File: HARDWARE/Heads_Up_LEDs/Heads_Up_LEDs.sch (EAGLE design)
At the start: 10 parts, among them J1 TRRS

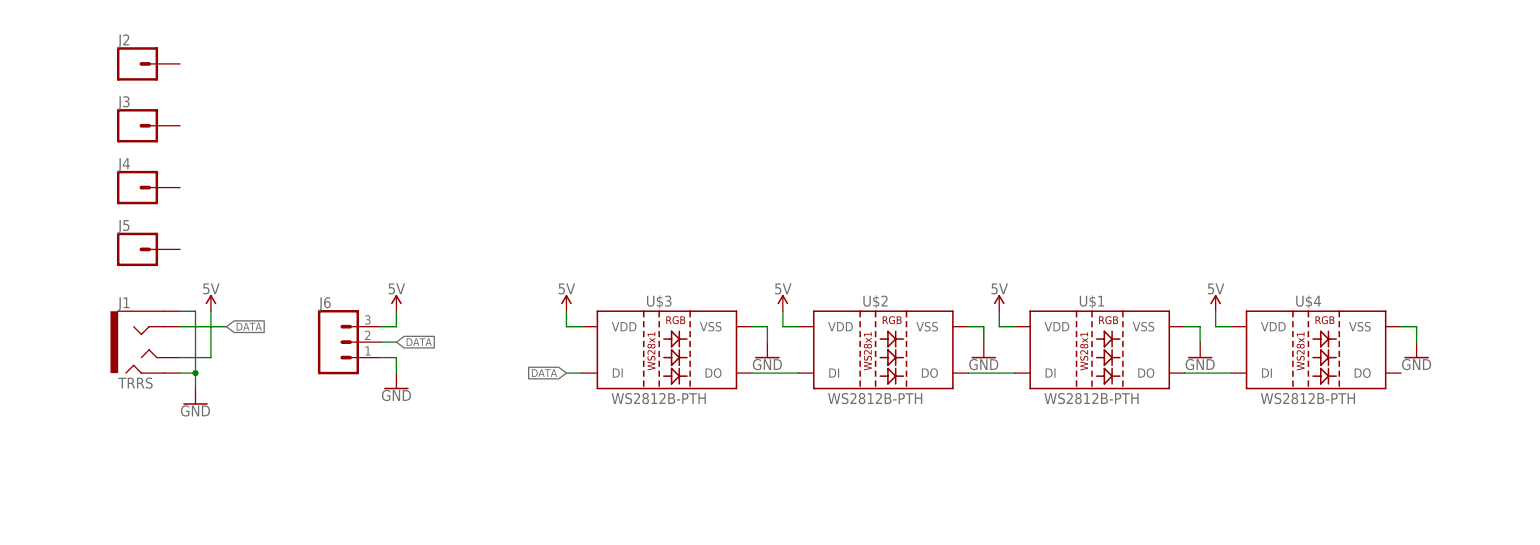
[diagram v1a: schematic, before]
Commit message: fixed ws2812 pinouts - added res and cap
library for ws2812 pth pinout was incorrect. I also added in a cap and resistor like the hookup guide suggests. Not sure if necessary, cuz the protos of v01 are working without (although I had to rotate the LEDs 180 degrees.
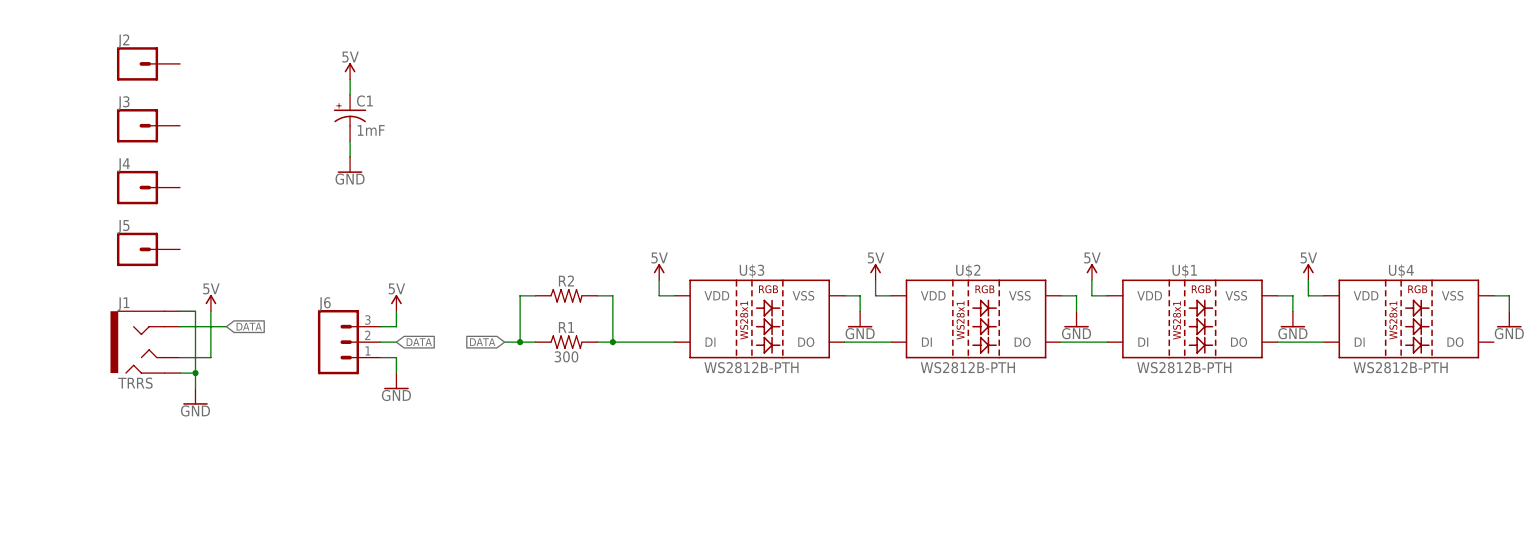
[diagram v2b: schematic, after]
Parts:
- added C1: 1mF, SparkFun-Capacitors:1000UF-RADIAL-5MM-25V-20%
- added R1: 300, SparkFun-Resistors:300OHM-0603-1/10W-1%
- added R2: (no value), SparkFun-Resistors:RESISTORAXIAL-0.3
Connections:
- new net N$2: R1.2, R2.2, U$3.DI
- net 5V: now also C1.+
- net DATA: now also R1.1, R2.1; no longer U$3.DI
- net GND: now also C1.-
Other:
- moved on the sheet: U$1, U$2, U$3, U$4
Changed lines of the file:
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@@
 <part name="SUPPLY6" library="SparkFun-PowerSymbols" deviceset="5V" device=""/>
 <part name="GND6" library="SparkFun-PowerSymbols" deviceset="GND" device=""/>
+<part name="R1" library="SparkFun-Resistors" deviceset="300OHM" device="-0603-1/10W-1%" value="300"/>
+<part name="R2" library="SparkFun-Resistors" deviceset="RESISTOR" device="AXIAL-0.3" value=" "/>
+<part name="C1" library="SparkFun-Capacitors" deviceset="1000UF" device="-RADIAL-5MM-25V-20%" value="1mF"/>
+<part name="GND7" library="SparkFun-PowerSymbols" deviceset="GND" device=""/>
+<part name="SUPPLY7" library="SparkFun-PowerSymbols" deviceset="5V" device=""/>
 </parts>
 <sheets>
@@
 <instances>
 <instance part="J1" gate="G$1" x="40.64" y="55.88"/>
-<instance part="U$1" gate="G$1" x="198.12" y="53.34"/>
-<instance part="U$2" gate="G$1" x="162.56" y="53.34"/>
-<instance part="U$3" gate="G$1" x="127" y="53.34"/>
+<instance part="U$1" gate="G$1" x="213.36" y="58.42"/>
+<instance part="U$2" gate="G$1" x="177.8" y="58.42"/>
+<instance part="U$3" gate="G$1" x="142.24" y="58.42"/>
 <instance part="J2" gate="G$1" x="38.1" y="101.6"/>
 <instance part="J3" gate="G$1" x="38.1" y="91.44"/>
@@
 <instance part="J5" gate="G$1" x="38.1" y="71.12"/>
 <instance part="J6" gate="J$1" x="71.12" y="55.88"/>
-<instance part="SUPPLY1" gate="G$1" x="109.22" y="60.96"/>
-<instance part="SUPPLY2" gate="G$1" x="144.78" y="60.96"/>
-<instance part="SUPPLY3" gate="G$1" x="180.34" y="60.96"/>
+<instance part="SUPPLY1" gate="G$1" x="124.46" y="66.04"/>
+<instance part="SUPPLY2" gate="G$1" x="160.02" y="66.04"/>
+<instance part="SUPPLY3" gate="G$1" x="195.58" y="66.04"/>
 <instance part="SUPPLY4" gate="G$1" x="50.8" y="60.96"/>
 <instance part="GND1" gate="1" x="48.26" y="45.72"/>
-<instance part="GND2" gate="1" x="142.24" y="53.34"/>
-<instance part="GND3" gate="1" x="177.8" y="53.34"/>
-<instance part="GND4" gate="1" x="213.36" y="53.34"/>
+<instance part="GND2" gate="1" x="157.48" y="58.42"/>
+<instance part="GND3" gate="1" x="193.04" y="58.42"/>
+<instance part="GND4" gate="1" x="228.6" y="58.42"/>
 <instance part="GND5" gate="1" x="81.28" y="48.26"/>
 <instance part="SUPPLY5" gate="G$1" x="81.28" y="60.96"/>
-<instance part="U$4" gate="G$1" x="233.68" y="53.34"/>
-<instance part="SUPPLY6" gate="G$1" x="215.9" y="60.96"/>
-<instance part="GND6" gate="1" x="248.92" y="53.34"/>
+<instance part="U$4" gate="G$1" x="248.92" y="58.42"/>
+<instance part="SUPPLY6" gate="G$1" x="231.14" y="66.04"/>
+<instance part="GND6" gate="1" x="264.16" y="58.42"/>
+<instance part="R1" gate="G$1" x="109.22" y="55.88"/>
+<instance part="R2" gate="G$1" x="109.22" y="63.5"/>
+<instance part="C1" gate="G$1" x="73.66" y="93.98"/>
+<instance part="GND7" gate="1" x="73.66" y="83.82"/>
+<instance part="SUPPLY7" gate="G$1" x="73.66" y="99.06"/>
 </instances>
 <busses>
@@
 <pinref part="U$3" gate="G$1" pin="DO"/>
 <pinref part="U$2" gate="G$1" pin="DI"/>
-<wire x1="139.7" y1="50.8" x2="147.32" y2="50.8" width="0.1524" layer="91"/>
+<wire x1="154.94" y1="55.88" x2="162.56" y2="55.88" width="0.1524" layer="91"/>
 </segment>
 </net>
@@
 <pinref part="U$2" gate="G$1" pin="DO"/>
 <pinref part="U$1" gate="G$1" pin="DI"/>
-<wire x1="175.26" y1="50.8" x2="182.88" y2="50.8" width="0.1524" layer="91"/>
+<wire x1="190.5" y1="55.88" x2="198.12" y2="55.88" width="0.1524" layer="91"/>
 </segment>
 </net>
@@
 <segment>
 <pinref part="U$3" gate="G$1" pin="VDD"/>
-<wire x1="111.76" y1="58.42" x2="109.22" y2="58.42" width="0.1524" layer="91"/>
-<wire x1="109.22" y1="58.42" x2="109.22" y2="60.96" width="0.1524" layer="91"/>
+<wire x1="127" y1="63.5" x2="124.46" y2="63.5" width="0.1524" layer="91"/>
+<wire x1="124.46" y1="63.5" x2="124.46" y2="66.04" width="0.1524" layer="91"/>
 <pinref part="SUPPLY1" gate="G$1" pin="5V"/>
 </segment>
 <segment>
 <pinref part="U$2" gate="G$1" pin="VDD"/>
-<wire x1="147.32" y1="58.42" x2="144.78" y2="58.42" width="0.1524" layer="91"/>
-<wire x1="144.78" y1="58.42" x2="144.78" y2="60.96" width="0.1524" layer="91"/>
+<wire x1="162.56" y1="63.5" x2="160.02" y2="63.5" width="0.1524" layer="91"/>
+<wire x1="160.02" y1="63.5" x2="160.02" y2="66.04" width="0.1524" layer="91"/>
 <pinref part="SUPPLY2" gate="G$1" pin="5V"/>
 </segment>
 <segment>
 <pinref part="U$1" gate="G$1" pin="VDD"/>
-<wire x1="182.88" y1="58.42" x2="180.34" y2="58.42" width="0.1524" layer="91"/>
-<wire x1="180.34" y1="58.42" x2="180.34" y2="60.96" width="0.1524" layer="91"/>
+<wire x1="198.12" y1="63.5" x2="195.58" y2="63.5" width="0.1524" layer="91"/>
+<wire x1="195.58" y1="63.5" x2="195.58" y2="66.04" width="0.1524" layer="91"/>
 <pinref part="SUPPLY3" gate="G$1" pin="5V"/>
 </segment>
@@
 <segment>
 <pinref part="U$4" gate="G$1" pin="VDD"/>
-<wire x1="218.44" y1="58.42" x2="215.9" y2="58.42" width="0.1524" layer="91"/>
-<wire x1="215.9" y1="58.42" x2="215.9" y2="60.96" width="0.1524" layer="91"/>
+<wire x1="233.68" y1="63.5" x2="231.14" y2="63.5" width="0.1524" layer="91"/>
+<wire x1="231.14" y1="63.5" x2="231.14" y2="66.04" width="0.1524" layer="91"/>
 <pinref part="SUPPLY6" gate="G$1" pin="5V"/>
+</segment>
+<segment>
+<pinref part="SUPPLY7" gate="G$1" pin="5V"/>
+<wire x1="73.66" y1="96.52" x2="73.66" y2="99.06" width="0.1524" layer="91"/>
+<pinref part="C1" gate="G$1" pin="+"/>
 </segment>
 </net>
@@
 <segment>
 <pinref part="U$3" gate="G$1" pin="VSS"/>
-<wire x1="139.7" y1="58.42" x2="142.24" y2="58.42" width="0.1524" layer="91"/>
-<wire x1="142.24" y1="58.42" x2="142.24" y2="55.88" width="0.1524" layer="91"/>
+<wire x1="154.94" y1="63.5" x2="157.48" y2="63.5" width="0.1524" layer="91"/>
+<wire x1="157.48" y1="63.5" x2="157.48" y2="60.96" width="0.1524" layer="91"/>
 <pinref part="GND2" gate="1" pin="GND"/>
 </segment>
 <segment>
 <pinref part="U$2" gate="G$1" pin="VSS"/>
-<wire x1="175.26" y1="58.42" x2="177.8" y2="58.42" width="0.1524" layer="91"/>
-<wire x1="177.8" y1="58.42" x2="177.8" y2="55.88" width="0.1524" layer="91"/>
+<wire x1="190.5" y1="63.5" x2="193.04" y2="63.5" width="0.1524" layer="91"/>
+<wire x1="193.04" y1="63.5" x2="193.04" y2="60.96" width="0.1524" layer="91"/>
 <pinref part="GND3" gate="1" pin="GND"/>
 </segment>
 <segment>
 <pinref part="U$1" gate="G$1" pin="VSS"/>
-<wire x1="210.82" y1="58.42" x2="213.36" y2="58.42" width="0.1524" layer="91"/>
-<wire x1="213.36" y1="58.42" x2="213.36" y2="55.88" width="0.1524" layer="91"/>
+<wire x1="226.06" y1="63.5" x2="228.6" y2="63.5" width="0.1524" layer="91"/>
+<wire x1="228.6" y1="63.5" x2="228.6" y2="60.96" width="0.1524" layer="91"/>
 <pinref part="GND4" gate="1" pin="GND"/>
 </segment>
@@
 <segment>
 <pinref part="U$4" gate="G$1" pin="VSS"/>
-<wire x1="246.38" y1="58.42" x2="248.92" y2="58.42" width="0.1524" layer="91"/>
-<wire x1="248.92" y1="58.42" x2="248.92" y2="55.88" width="0.1524" layer="91"/>
+<wire x1="261.62" y1="63.5" x2="264.16" y2="63.5" width="0.1524" layer="91"/>
+<wire x1="264.16" y1="63.5" x2="264.16" y2="60.96" width="0.1524" layer="91"/>
 <pinref part="GND6" gate="1" pin="GND"/>
+</segment>
+<segment>
+<pinref part="C1" gate="G$1" pin="-"/>
+<pinref part="GND7" gate="1" pin="GND"/>
+<wire x1="73.66" y1="86.36" x2="73.66" y2="88.9" width="0.1524" layer="91"/>
 </segment>
 </net>
 <net name="DATA" class="0">
-<segment>
-<pinref part="U$3" gate="G$1" pin="DI"/>
-<wire x1="111.76" y1="50.8" x2="109.22" y2="50.8" width="0.1524" layer="91"/>
-<label x="109.22" y="50.8" size="1.27" layer="95" rot="R180" xref="yes"/>
-</segment>
 <segment>
 <pinref part="J6" gate="J$1" pin="2"/>
@@
 <label x="53.34" y="58.42" size="1.27" layer="95" xref="yes"/>
 </segment>
+<segment>
+<wire x1="104.14" y1="55.88" x2="101.6" y2="55.88" width="0.1524" layer="91"/>
+<label x="99.06" y="55.88" size="1.27" layer="95" rot="R180" xref="yes"/>
+<pinref part="R1" gate="G$1" pin="1"/>
+<pinref part="R2" gate="G$1" pin="1"/>
+<wire x1="101.6" y1="55.88" x2="99.06" y2="55.88" width="0.1524" layer="91"/>
+<wire x1="104.14" y1="63.5" x2="101.6" y2="63.5" width="0.1524" layer="91"/>
+<wire x1="101.6" y1="63.5" x2="101.6" y2="55.88" width="0.1524" layer="91"/>
+<junction x="101.6" y="55.88"/>
+</segment>
 </net>
 <net name="N$1" class="0">
@@
 <pinref part="U$1" gate="G$1" pin="DO"/>
 <pinref part="U$4" gate="G$1" pin="DI"/>
-<wire x1="210.82" y1="50.8" x2="218.44" y2="50.8" width="0.1524" layer="91"/>
+<wire x1="226.06" y1="55.88" x2="233.68" y2="55.88" width="0.1524" layer="91"/>
 </segment>
 </net>
+<net name="N$2" class="0">
+<segment>
+<pinref part="U$3" gate="G$1" pin="DI"/>
+<pinref part="R1" gate="G$1" pin="2"/>
+<wire x1="127" y1="55.88" x2="116.84" y2="55.88" width="0.1524" layer="91"/>
+<wire x1="116.84" y1="55.88" x2="114.3" y2="55.88" width="0.1524" layer="91"/>
+<wire x1="116.84" y1="55.88" x2="116.84" y2="63.5" width="0.1524" layer="91"/>
+<junction x="116.84" y="55.88"/>
+<pinref part="R2" gate="G$1" pin="2"/>
+<wire x1="116.84" y1="63.5" x2="114.3" y2="63.5" width="0.1524" layer="91"/>
+</segment>
+</net>
